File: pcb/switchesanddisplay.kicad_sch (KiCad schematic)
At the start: 14 parts, among them J6 ${FAMILY}, SW2 SW_Push, SW3 SW_Push, SW4 SW_Push, SW5 SW_Push, SW6 SW_Push, SW7 SW_Push, SW8 SW_Push, SW9 SW_Push, U2 ER_OLEDM0.91_1x-I2C

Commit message: Finish the schematic ig
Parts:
- removed J?: ${FAMILY}, symbol Connectors:Connector 4 Female
- added J12: ${FAMILY}, symbol Connectors:Connector 4 Female
- gave numbers to parts that had none: 3
- renumbered J6 to J9
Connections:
- net GND: now also J9.1, J12.2; no longer J9.4
- net at U2.2 (VCC): now also J9.2; no longer J9.1
- net at U2.3 (SCL): now also J9.4; no longer J9.2
- net at SW1.A: now also J12.1
- net at SW1.B: now also J12.3
- net at SW1.S1: now also J12.4

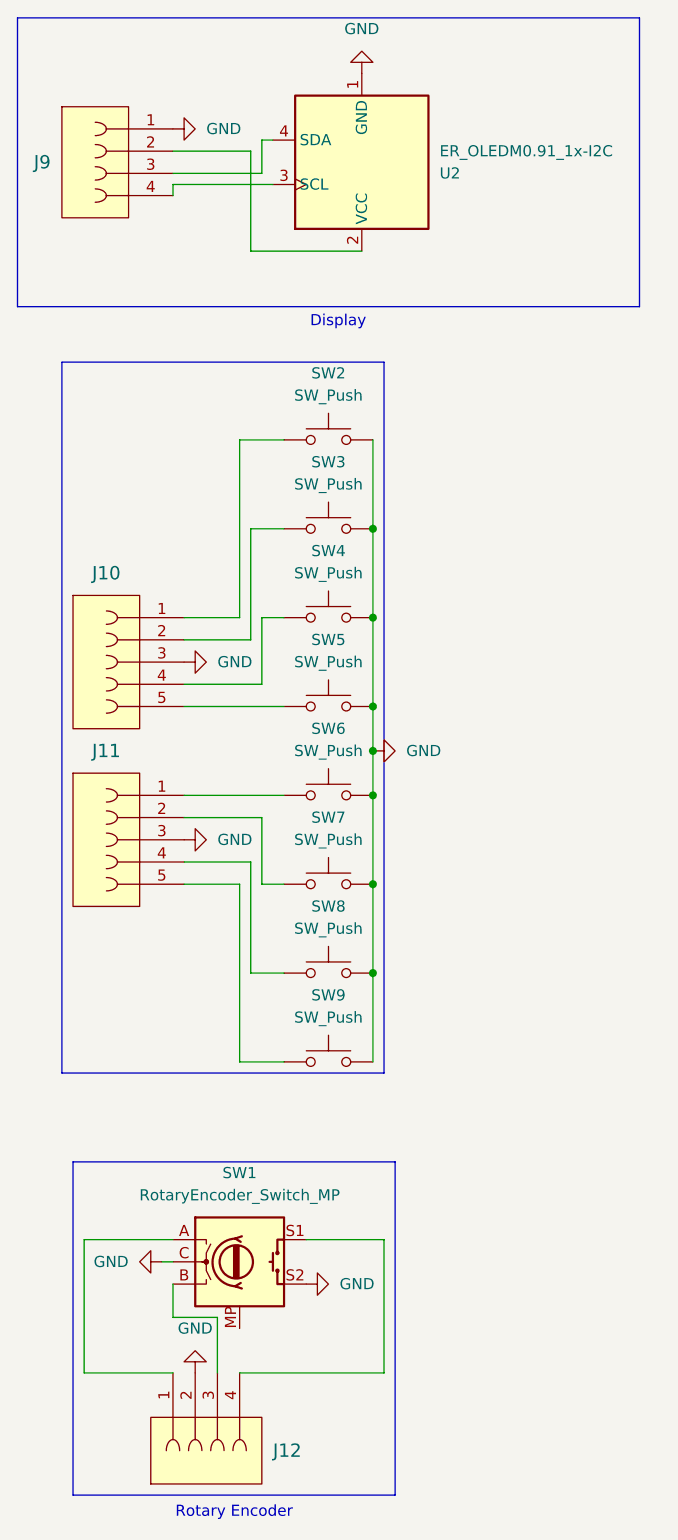
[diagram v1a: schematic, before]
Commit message: Ground should point downwards so i fixed that
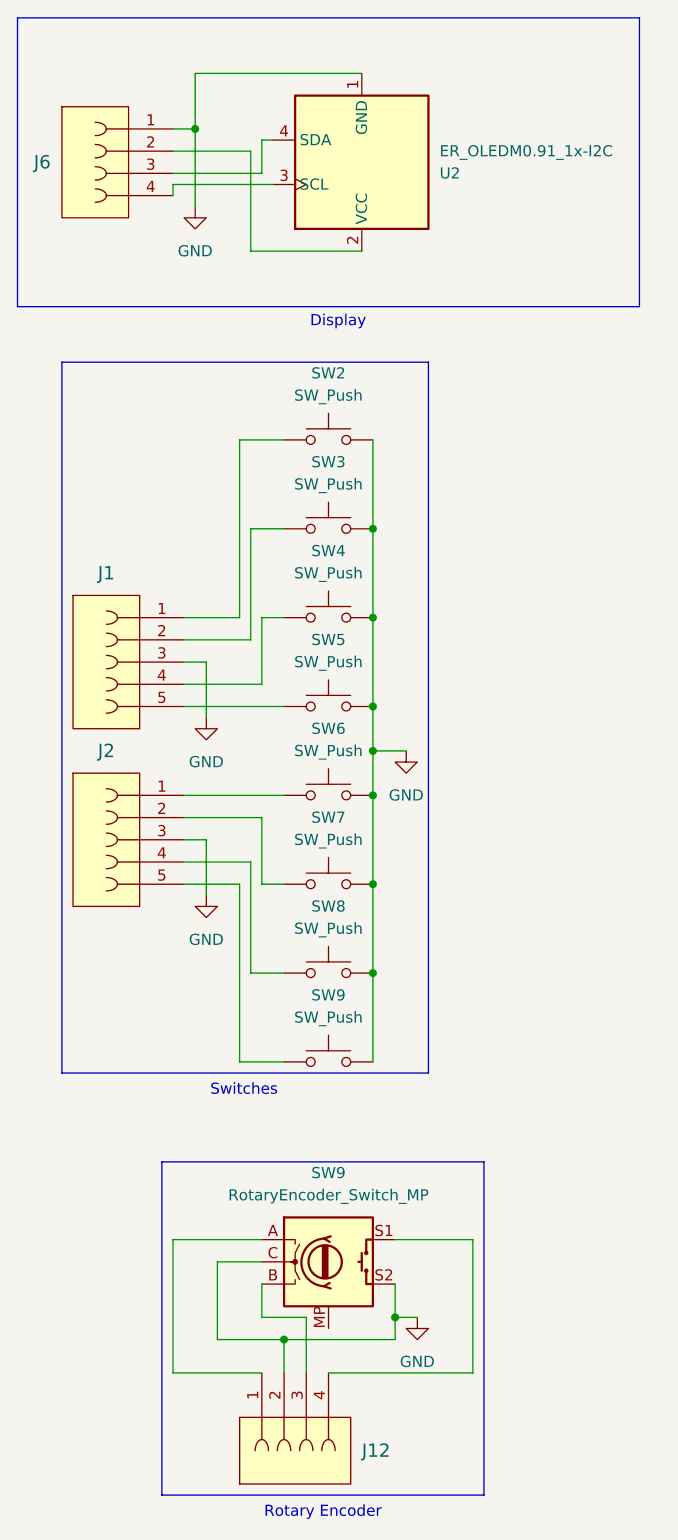
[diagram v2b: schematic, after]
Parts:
- removed SW1: RotaryEncoder_Switch_MP, symbol Device:RotaryEncoder_Switch_MP
- added SW9: RotaryEncoder_Switch_MP, Rotary_Encoder:RotaryEncoder_Alps_EC11E-Switch_Vertical_H20mm_MountingHoles, symbol Device:RotaryEncoder_Switch_MP
- J1: renamed from J10; footprint (none) -> Connector_JST:JST_XH_B5B-XH-A_1x05_P2.50mm_Vertical
- J12: footprint (none) -> Connector_JST:JST_XH_B4B-XH-A_1x04_P2.50mm_Vertical
- J2: renamed from J11; footprint (none) -> Connector_JST:JST_XH_B5B-XH-A_1x05_P2.50mm_Vertical
- J6: renamed from J9; footprint (none) -> Connector_JST:JST_XH_B4B-XH-A_1x04_P2.50mm_Vertical
- SW2, SW3, SW4, SW5, SW6, SW7, SW8, SW9: footprint (none) -> Button_Switch_Keyboard:SW_Cherry_MX_1.00u_PCB
- U2: footprint Display:ER_OLEDM0.91_1x-I2C -> Connector_JST:JST_XH_B4B-XH-A_1x04_P2.50mm_Vertical
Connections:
- net GND: now also SW9.C, SW9.S2
- net at J12.1: now also SW9.A
- net at J12.3: now also SW9.B
- net at J12.4: now also SW9.S1
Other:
- note added: "Switches"
- moved on the sheet: J12

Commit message: Wire up the schematic for the switches
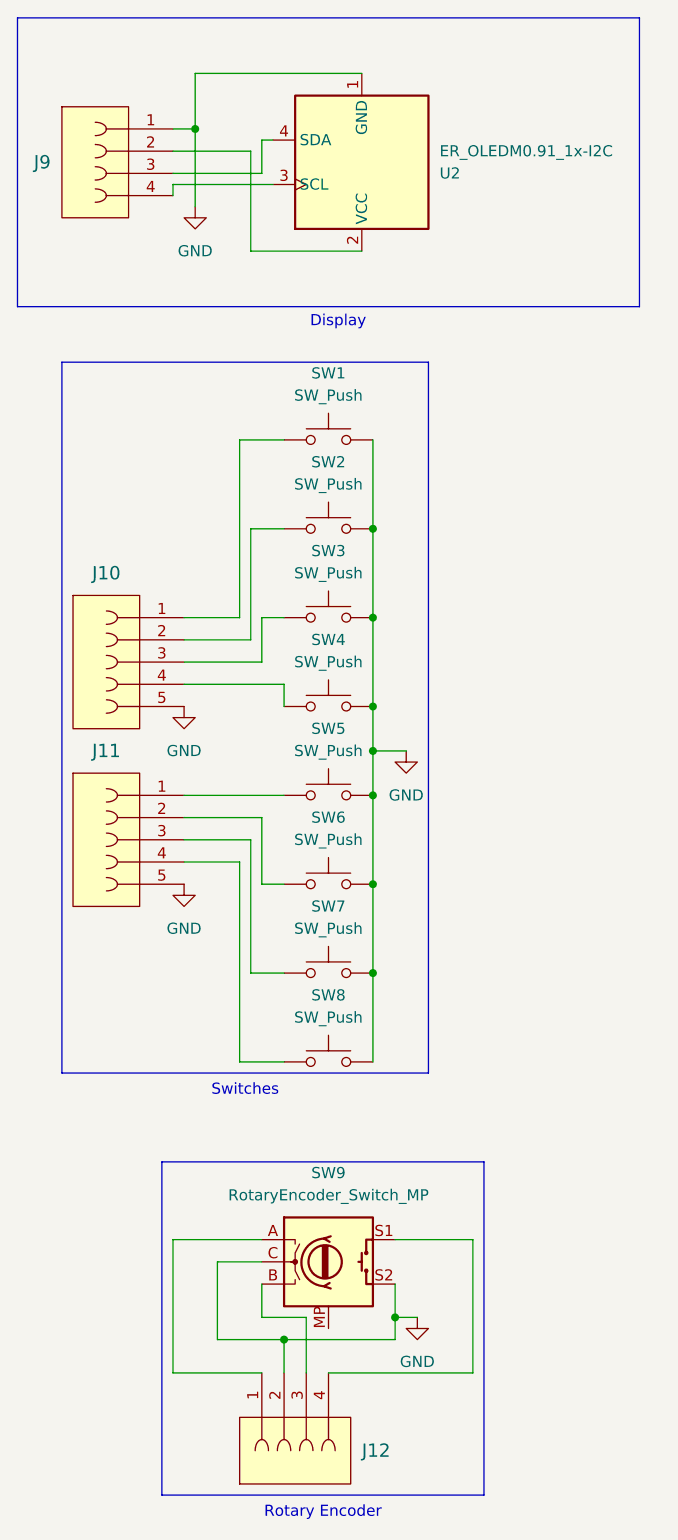
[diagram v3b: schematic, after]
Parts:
- renumbered J1 to J10, J2 to J11, J6 to J9, SW2 to SW1, SW3 to SW2, SW4 to SW3, SW5 to SW4, SW6 to SW5, SW7 to SW6, SW8 to SW7, SW9 to SW8
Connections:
- net GND: now also J10.5, J11.5; no longer J10.3, J11.3
- net at SW7.1: now also J11.3; no longer J11.4
- net at SW3.1: now also J10.3; no longer J10.4
- net at SW4.1: now also J10.4; no longer J10.5
- net at SW8.1: now also J11.4; no longer J11.5

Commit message: Fix the 46 ERC rules
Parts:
- removed J10, J11: ${FAMILY}, Connector_JST:JST_XH_B5B-XH-A_1x05_P2.50mm_Vertical, symbol Connectors:Connector 5 Female
- removed J12, J9: ${FAMILY}, Connector_JST:JST_XH_B4B-XH-A_1x04_P2.50mm_Vertical, symbol Connectors:Connector 4 Female
- added J?: EncoderConnector, symbol Connector_Generic:Conn_01x04
- added J?: LeftKeyConnector, symbol Connector_Generic:Conn_01x05
- added J?: DisplayConnector, symbol Connector_Generic:Conn_01x04
- added J?: RightKeyConnector, symbol Connector_Generic:Conn_01x05
- SW9: footprint Rotary_Encoder:RotaryEncoder_Alps_EC11E-Switch_Vertical_H20mm_MountingHoles -> Rotary_Encoder:RotaryEncoder_Alps_EC11E-Switch_Vertical_H20mm
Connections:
- net GND: now also J?.1 (Pin_1), J?.4 (Pin_4), J?.5 (Pin_5), J?.5 (Pin_5)
- net at U2.2 (VCC): now also J?.2 (Pin_2)
- net at U2.4 (SDA): now also J?.3 (Pin_3)
- net at U2.3 (SCL): now also J?.4 (Pin_4)
- net at SW9.A: now also J?.3 (Pin_3)
- net at SW9.B: now also J?.2 (Pin_2)
- net at SW9.S1: now also J?.1 (Pin_1)
- net at SW5.1: now also J?.1 (Pin_1)
- net at SW7.1: now also J?.3 (Pin_3)
- net at SW1.1: now also J?.1 (Pin_1)
- net at SW2.1: now also J?.2 (Pin_2)
- net at SW3.1: now also J?.3 (Pin_3)
- net at SW4.1: now also J?.4 (Pin_4)
- net at SW8.1: now also J?.4 (Pin_4)
- net at SW6.1: now also J?.2 (Pin_2)
- no-connect marks 0 -> 1
